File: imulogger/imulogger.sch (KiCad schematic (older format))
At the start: 31 parts, among them J1 DEBUG, J2 BATCONN, J4 Micro_SD_Card, J5 PWRCONN, Q1 TP0610T, U1 ESP32-WROOM-32, U2 USFS, U3 MCP1826S, U4 MCP73831-2-OT

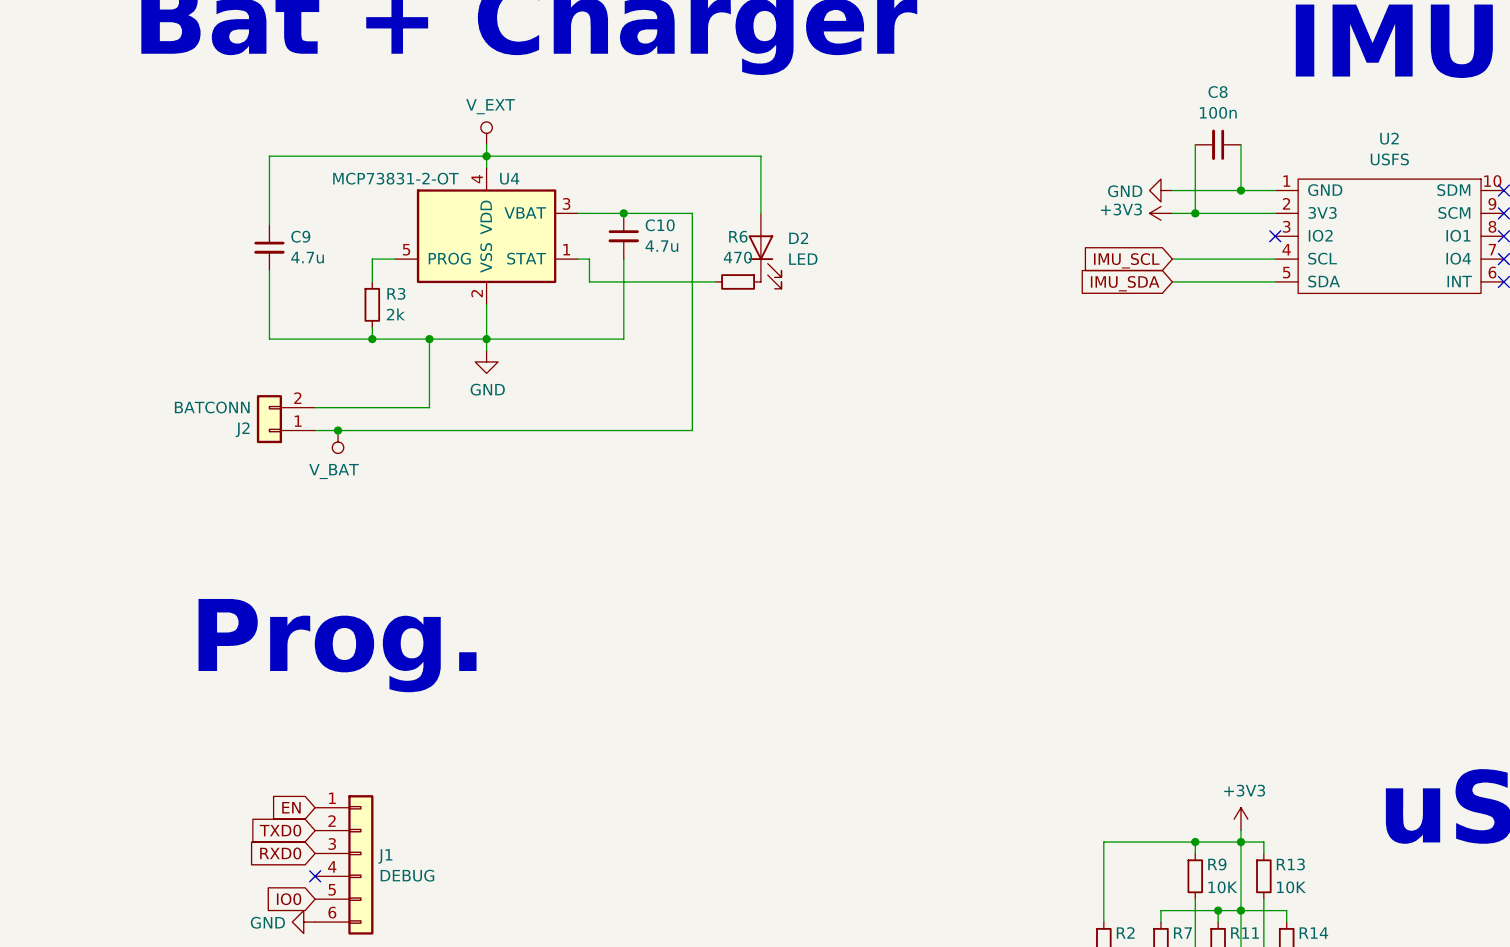
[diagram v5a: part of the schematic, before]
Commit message: imulogger: add battery protection circuit
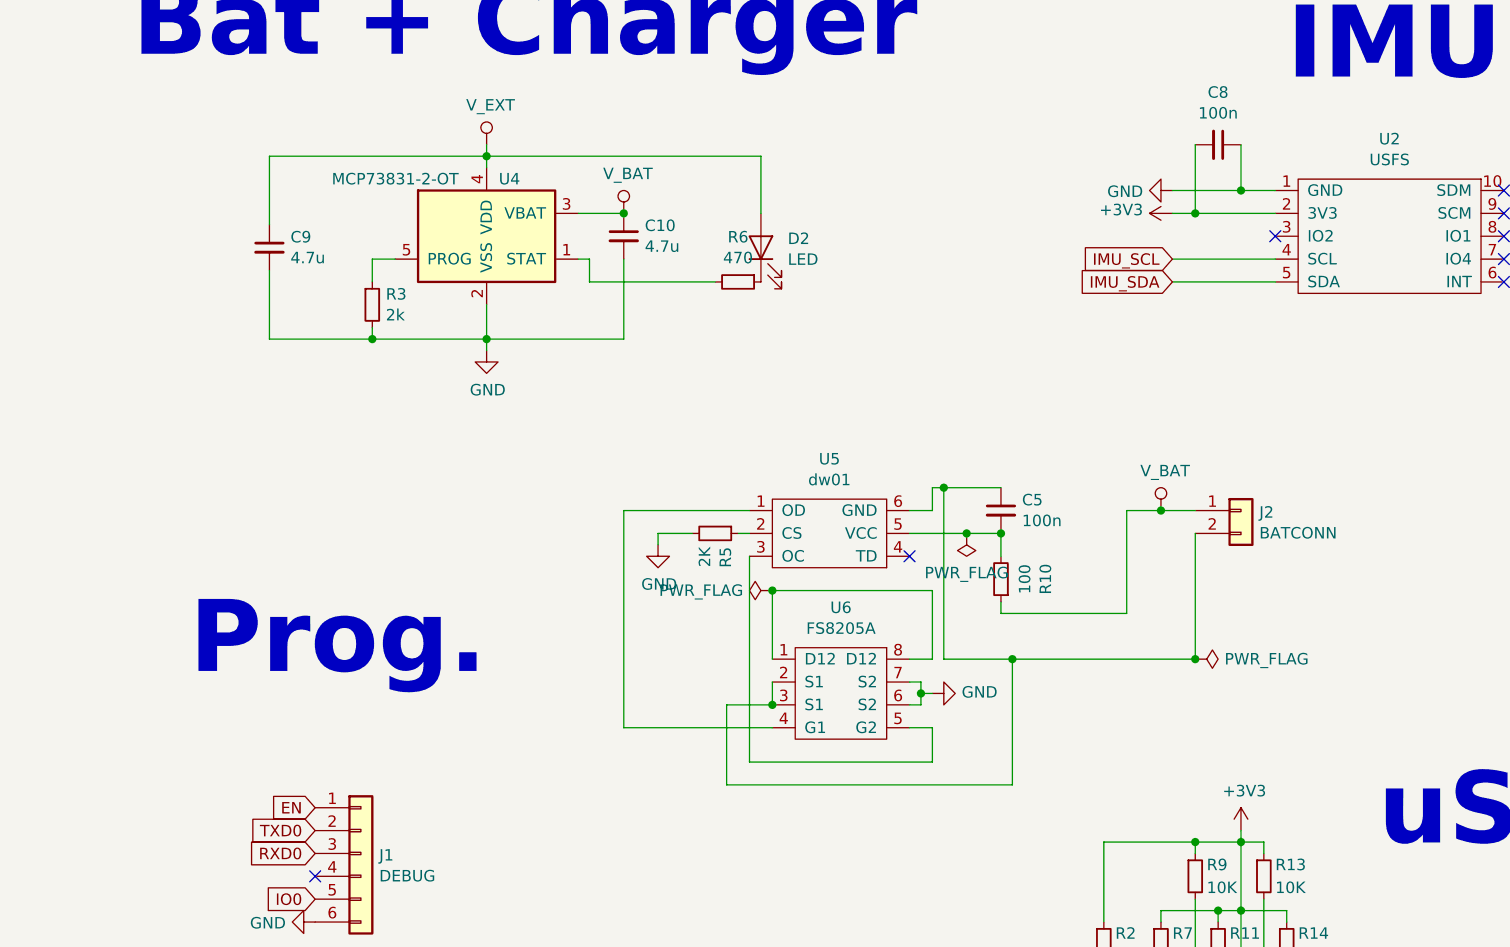
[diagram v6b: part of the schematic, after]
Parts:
- added C5: 100n, Capacitor_SMD:C_0805_2012Metric_Pad1.15x1.40mm_HandSolder, symbol Device:C_Small
- added R10: 100, Resistor_SMD:R_0805_2012Metric_Pad1.15x1.40mm_HandSolder, symbol Device:R_Small
- added R5: 2K, Resistor_SMD:R_0805_2012Metric_Pad1.15x1.40mm_HandSolder, symbol Device:R_Small
- added U5: dw01, Package_TO_SOT_SMD:SOT-23-6_Handsoldering, symbol imulogger-symbols:dw01
- added U6: FS8205A, Package_SO:TSSOP-8_4.4x3mm_P0.65mm, symbol imulogger-symbols:FS8205A
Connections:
- net GND: now also R5.2, U6.6 (S2), U6.7 (S2); no longer J2.2 (Pin_2)
- net V_BAT: now also R10.1
- new net: C5.1, J2.2 (Pin_2), U5.6 (GND), U6.2 (S1), U6.3 (S1)
- new net: C5.2, R10.2, U5.5 (VCC)
- new net: R5.1, U5.2 (CS)
- new net: U6.1 (D12), U6.8 (D12)
- new net: U5.1 (OD), U6.4 (G1)
- new net: U5.3 (OC), U6.5 (G2)
- no-connect marks 30 -> 31
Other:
- moved on the sheet: J2
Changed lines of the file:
@@
 Text Notes 1050 6200 0    315  ~ 63
 PwrSrcSel + Reg
-$Comp
-L Connector_Generic:Conn_01x02 J2
-U 1 1 5CBEA1D0
-P 4500 2700
-F 0 "J2" H 4580 2692 50  0000 L CNN
-F 1 "BATCONN" H 4580 2601 50  0000 L CNN
-F 2 "Connector_PinHeader_2.54mm:PinHeader_1x02_P2.54mm_Vertical" H 4500 2700 50  0001 C CNN
-F 3 "~" H 4500 2700 50  0001 C CNN
-	1    4500 2700
-	-1   0    0    1
-$EndComp
-Wire Wire Line
-	5200 2600 5200 2300
-Wire Wire Line
-	4950 2300 5200 2300
-Wire Wire Line
-	5200 2300 5450 2300
-Connection ~ 5200 2300
-Wire Wire Line
-	6350 2700 6350 1750
-Wire Wire Line
-	6350 1750 6050 1750
 Connection ~ 6050 1750
-Wire Wire Line
-	4700 2700 4800 2700
 $Comp
 L Device:D_Schottky D4
@@
 L imulogger-symbols:V_BAT #PWR06
 U 1 1 5CCA121B
-P 4800 2700
-F 0 "#PWR06" H 4800 2550 50  0001 C CNN
-F 1 "V_BAT" H 4818 2873 50  0000 C CNN
-F 2 "" H 4800 2700 50  0001 C CNN
-F 3 "" H 4800 2700 50  0001 C CNN
-	1    4800 2700
-	-1   0    0    1
-$EndComp
-Connection ~ 4800 2700
+P 6050 1750
+F 0 "#PWR06" H 6050 1600 50  0001 C CNN
+F 1 "V_BAT" H 6068 1923 50  0000 C CNN
+F 2 "" H 6050 1750 50  0001 C CNN
+F 3 "" H 6050 1750 50  0001 C CNN
+	1    6050 1750
+	1    0    0    -1
+$EndComp
 $Comp
 L imulogger-symbols:V_EXT #PWR011
@@
 Wire Wire Line
 	1250 6900 1300 6900
-Wire Wire Line
-	4800 2700 6350 2700
-Wire Wire Line
-	4700 2600 5200 2600
 $Comp
 L power:PWR_FLAG #FLG0103
@@
 NoConn ~ 9050 6150
 NoConn ~ 9050 6250
+$Comp
+L Device:R_Small R10
+U 1 1 5CD8A10E
+P 7700 3350
+F 0 "R10" V 7504 3350 50  0000 C CNN
+F 1 "100" V 7595 3350 50  0000 C CNN
+F 2 "Resistor_SMD:R_0805_2012Metric_Pad1.15x1.40mm_HandSolder" H 7700 3350 50  0001 C CNN
+F 3 "~" H 7700 3350 50  0001 C CNN
+	1    7700 3350
+	-1   0    0    1
+$EndComp
+$Comp
+L Device:R_Small R5
+U 1 1 5CD8A55A
+P 6450 3150
+F 0 "R5" H 6509 3196 50  0000 L CNN
+F 1 "2K" H 6509 3105 50  0000 L CNN
+F 2 "Resistor_SMD:R_0805_2012Metric_Pad1.15x1.40mm_HandSolder" H 6450 3150 50  0001 C CNN
+F 3 "~" H 6450 3150 50  0001 C CNN
+	1    6450 3150
+	0    1    1    0
+$EndComp
+$Comp
+L Device:C_Small C5
+U 1 1 5CD8AEEA
+P 7700 3050
+F 0 "C5" H 7792 3096 50  0000 L CNN
+F 1 "100n" H 7792 3005 50  0000 L CNN
+F 2 "Capacitor_SMD:C_0805_2012Metric_Pad1.15x1.40mm_HandSolder" H 7700 3050 50  0001 C CNN
+F 3 "~" H 7700 3050 50  0001 C CNN
+	1    7700 3050
+	1    0    0    -1
+$EndComp
+$Comp
+L imulogger-symbols:FS8205A U6
+U 1 1 5CD95DDA
+P 7000 3850
+F 0 "U6" H 7000 4225 50  0000 C CNN
+F 1 "FS8205A" H 7000 4134 50  0000 C CNN
+F 2 "Package_SO:TSSOP-8_4.4x3mm_P0.65mm" H 7000 3850 50  0001 C CNN
+F 3 "" H 7000 3850 50  0001 C CNN
+	1    7000 3850
+	1    0    0    -1
+$EndComp
+$Comp
+L imulogger-symbols:dw01 U5
+U 1 1 5CD9CC1D
+P 6950 3150
+F 0 "U5" V 6625 3150 50  0000 C CNN
+F 1 "dw01" V 6716 3150 50  0000 C CNN
+F 2 "Package_TO_SOT_SMD:SOT-23-6_Handsoldering" H 6950 3150 50  0001 C CNN
+F 3 "" H 6950 3150 50  0001 C CNN
+	1    6950 3150
+	0    1    1    0
+$EndComp
+Wire Wire Line
+	7300 3050 7400 3050
+Wire Wire Line
+	7400 3050 7400 2950
+Wire Wire Line
+	7400 2950 7450 2950
+NoConn ~ 7300 3250
+Wire Wire Line
+	7700 3150 7700 3250
+Connection ~ 7700 3150
+Wire Wire Line
+	6600 3150 6550 3150
+$Comp
+L Connector_Generic:Conn_01x02 J2
+U 1 1 5CBEA1D0
+P 8750 3050
+F 0 "J2" H 8830 3042 50  0000 L CNN
+F 1 "BATCONN" H 8830 2951 50  0000 L CNN
+F 2 "Connector_PinHeader_2.54mm:PinHeader_1x02_P2.54mm_Vertical" H 8750 3050 50  0001 C CNN
+F 3 "~" H 8750 3050 50  0001 C CNN
+	1    8750 3050
+	1    0    0    -1
+$EndComp
+Wire Wire Line
+	8550 3050 8400 3050
+Wire Wire Line
+	8250 3050 8250 3500
+Wire Wire Line
+	8250 3500 7700 3500
+Wire Wire Line
+	7700 3500 7700 3450
+Wire Wire Line
+	4950 2300 5450 2300
+$Comp
+L imulogger-symbols:V_BAT #PWR014
+U 1 1 5CDD3FAE
+P 8400 3050
+F 0 "#PWR014" H 8400 2900 50  0001 C CNN
+F 1 "V_BAT" H 8418 3223 50  0000 C CNN
+F 2 "" H 8400 3050 50  0001 C CNN
+F 3 "" H 8400 3050 50  0001 C CNN
+	1    8400 3050
+	1    0    0    -1
+$EndComp
+Connection ~ 8400 3050
+Wire Wire Line
+	8400 3050 8250 3050
+Wire Wire Line
+	6600 3050 6050 3050
+Wire Wire Line
+	6050 4000 6700 4000
+Wire Wire Line
+	6600 4150 7400 4150
+Wire Wire Line
+	7400 4150 7400 4000
+Wire Wire Line
+	7400 4000 7300 4000
+$Comp
+L power:GND #PWR012
+U 1 1 5CDE1482
+P 6200 3200
+F 0 "#PWR012" H 6200 2950 50  0001 C CNN
+F 1 "GND" H 6205 3027 50  0000 C CNN
+F 2 "" H 6200 3200 50  0001 C CNN
+F 3 "" H 6200 3200 50  0001 C CNN
+	1    6200 3200
+	1    0    0    -1
+$EndComp
+Wire Wire Line
+	6350 3150 6200 3150
+Wire Wire Line
+	6200 3150 6200 3200
+Wire Wire Line
+	8550 3150 8550 3700
+Wire Wire Line
+	8550 3700 7750 3700
+Wire Wire Line
+	7750 3700 7750 4250
+Wire Wire Line
+	7750 4250 6500 4250
+Wire Wire Line
+	6500 4250 6500 3900
+Wire Wire Line
+	6500 3900 6700 3900
+Wire Wire Line
+	6700 3800 6700 3900
+Connection ~ 6700 3900
+Wire Wire Line
+	7300 3700 7400 3700
+Wire Wire Line
+	7400 3700 7400 3400
+Wire Wire Line
+	7400 3400 6700 3400
+Wire Wire Line
+	6700 3400 6700 3700
+$Comp
+L power:GND #PWR013
+U 1 1 5CDF671F
+P 7400 3850
+F 0 "#PWR013" H 7400 3600 50  0001 C CNN
+F 1 "GND" V 7405 3722 50  0000 R CNN
+F 2 "" H 7400 3850 50  0001 C CNN
+F 3 "" H 7400 3850 50  0001 C CNN
+	1    7400 3850
+	0    -1   -1   0
+$EndComp
+Wire Wire Line
+	7300 3800 7350 3800
+Wire Wire Line
+	7350 3800 7350 3850
+Wire Wire Line
+	7350 3850 7400 3850
+Wire Wire Line
+	7300 3900 7350 3900
+Wire Wire Line
+	7350 3900 7350 3850
+Connection ~ 7350 3850
+$Comp
+L power:PWR_FLAG #FLG0105
+U 1 1 5CE03E12
+P 8550 3700
+F 0 "#FLG0105" H 8550 3775 50  0001 C CNN
+F 1 "PWR_FLAG" V 8550 3828 50  0000 L CNN
+F 2 "" H 8550 3700 50  0001 C CNN
+F 3 "~" H 8550 3700 50  0001 C CNN
+	1    8550 3700
+	0    1    1    0
+$EndComp
+Wire Wire Line
+	7450 3700 7750 3700
+Connection ~ 7450 2950
+Wire Wire Line
+	7450 2950 7700 2950
+Connection ~ 7750 3700
+Connection ~ 8550 3700
+Wire Wire Line
+	7450 2950 7450 3700
+Wire Wire Line
+	7700 3150 7550 3150
+$Comp
+L power:PWR_FLAG #FLG0106
+U 1 1 5CE0DB17
+P 7550 3150
+F 0 "#FLG0106" H 7550 3225 50  0001 C CNN
+F 1 "PWR_FLAG" H 7550 3323 50  0000 C CNN
+F 2 "" H 7550 3150 50  0001 C CNN
+F 3 "~" H 7550 3150 50  0001 C CNN
+	1    7550 3150
+	-1   0    0    1
+$EndComp
+Connection ~ 7550 3150
+Wire Wire Line
+	7550 3150 7300 3150
+Wire Wire Line
+	6050 3050 6050 4000
+Wire Wire Line
+	6600 3250 6600 4150
+$Comp
+L power:PWR_FLAG #FLG0107
+U 1 1 5CE12164
+P 6700 3400
+F 0 "#FLG0107" H 6700 3475 50  0001 C CNN
+F 1 "PWR_FLAG" V 6700 3527 50  0000 L CNN
+F 2 "" H 6700 3400 50  0001 C CNN
+F 3 "~" H 6700 3400 50  0001 C CNN
+	1    6700 3400
+	0    -1   -1   0
+$EndComp
+Connection ~ 6700 3400
 $EndSCHEMATC

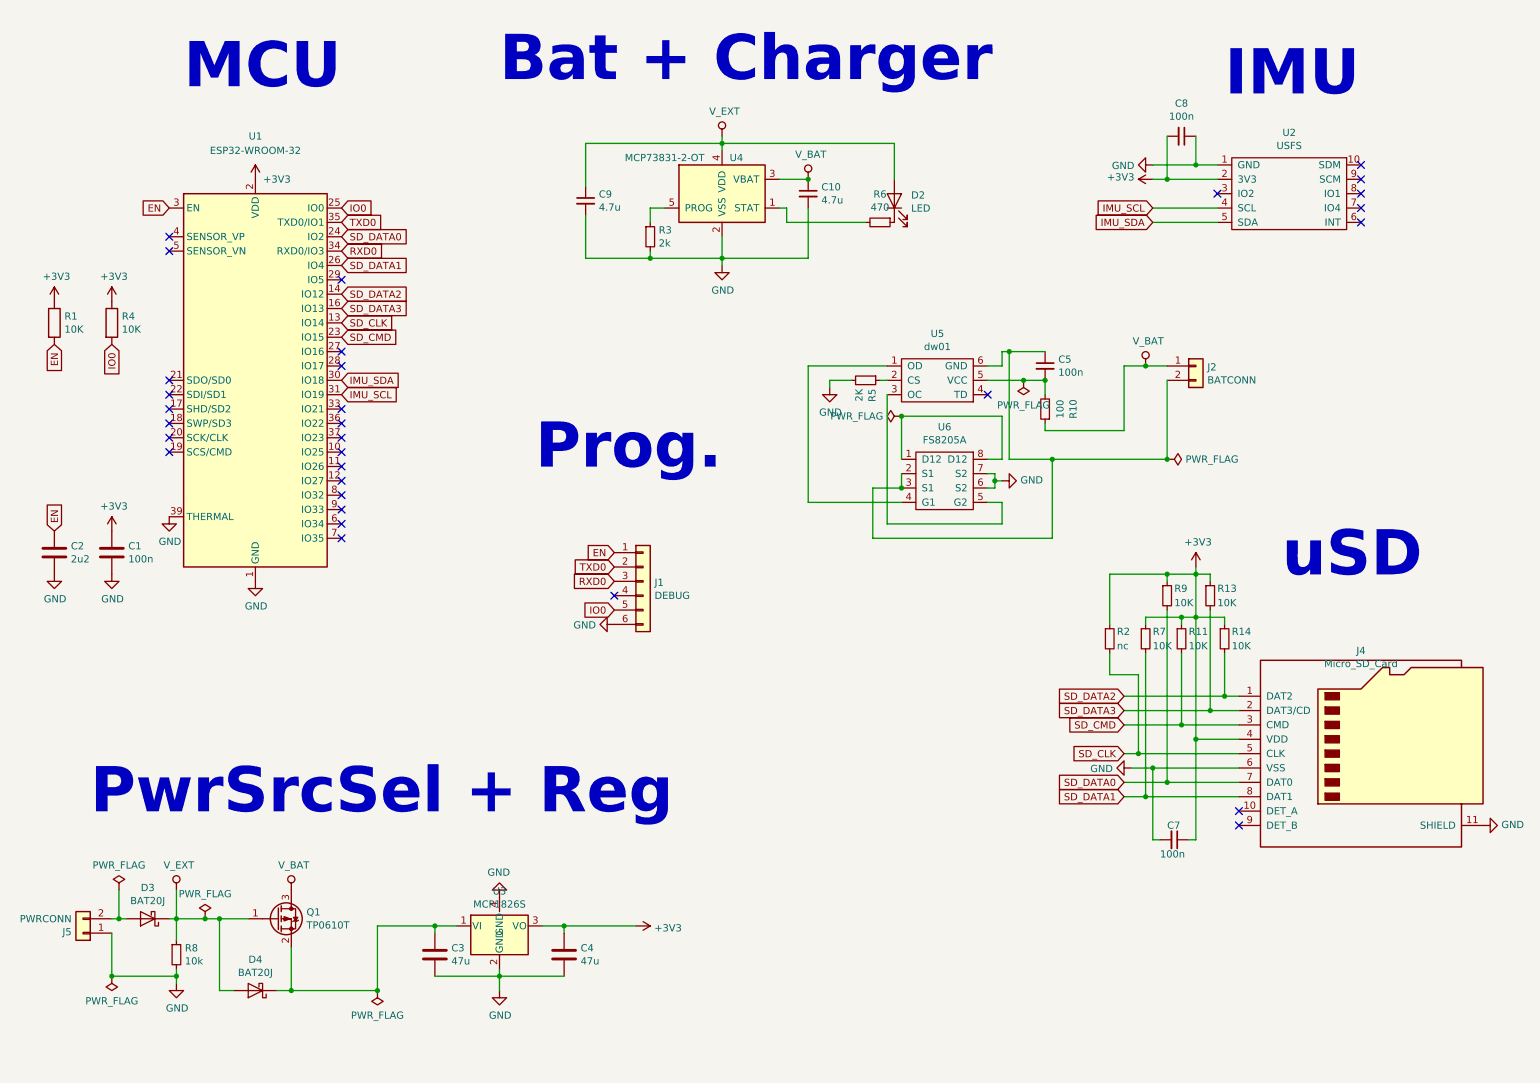
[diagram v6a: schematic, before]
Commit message: remove charger and add switch and JST socket
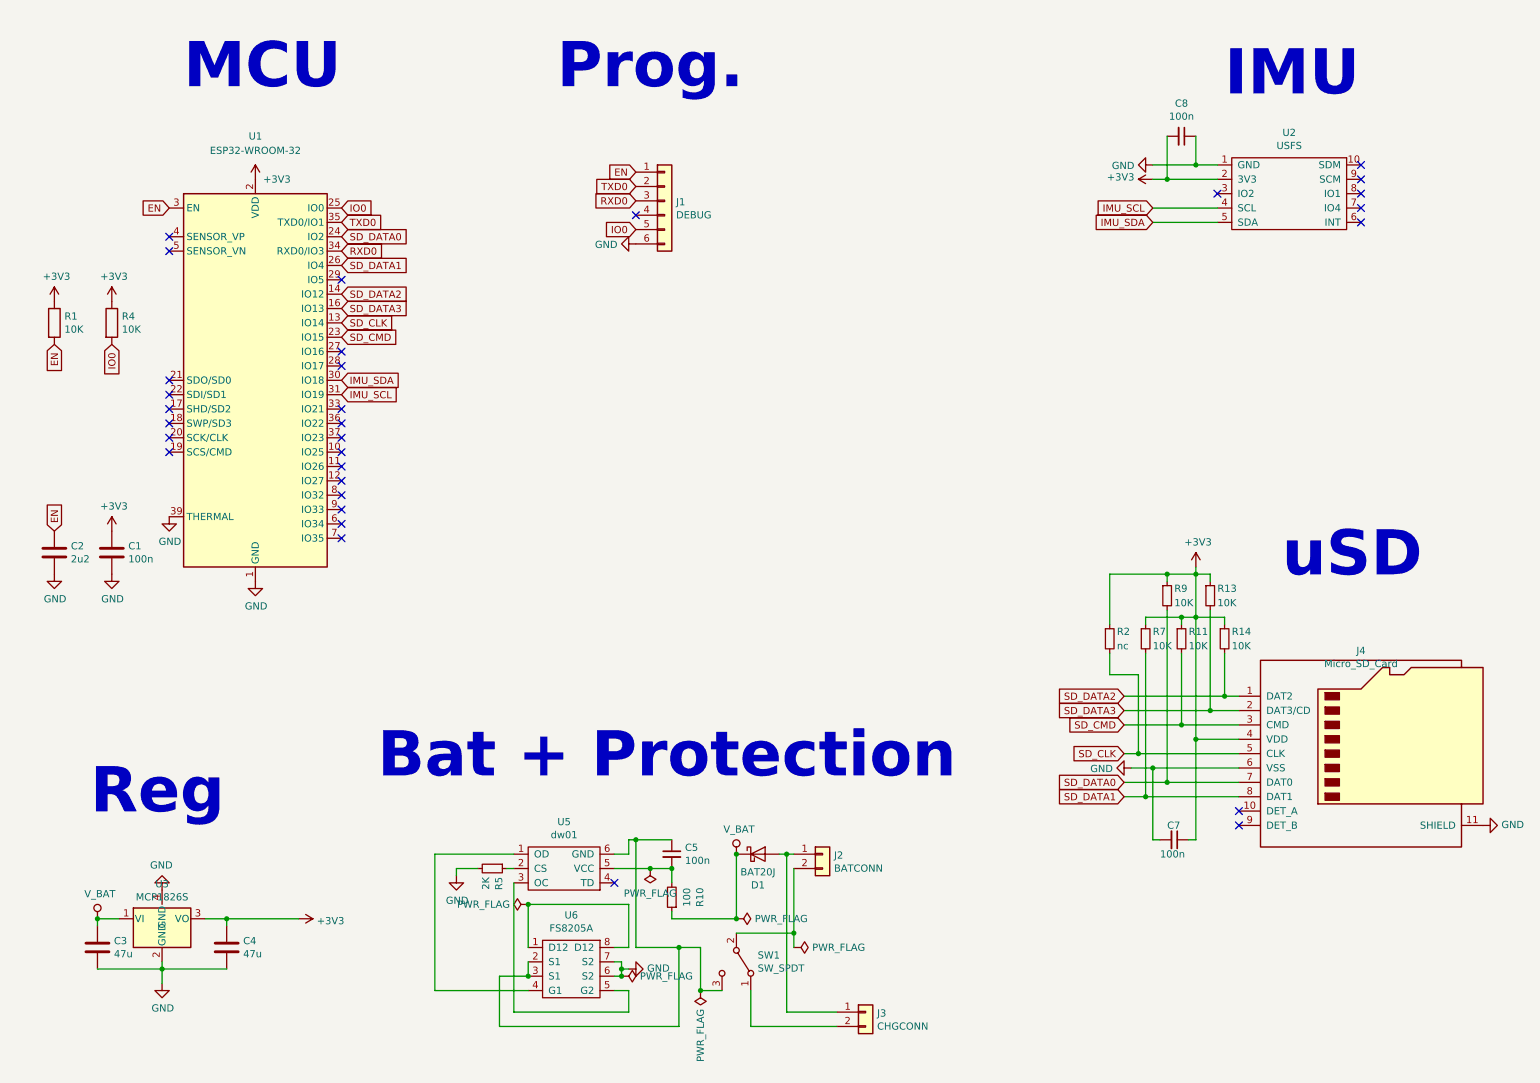
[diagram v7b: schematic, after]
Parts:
- removed C10, C9: 4.7u, Capacitor_SMD:C_0805_2012Metric_Pad1.15x1.40mm_HandSolder, symbol Device:C_Small
- removed D2: LED, LED_SMD:LED_0805_2012Metric_Pad1.15x1.40mm_HandSolder, symbol Device:LED
- removed D3, D4: BAT20J, Diode_SMD:D_SOD-323, symbol Device:D_Schottky
- removed J5: PWRCONN, Connector_PinHeader_2.54mm:PinHeader_1x02_P2.54mm_Vertical, symbol Connector_Generic:Conn_01x02
- removed Q1: TP0610T, Package_TO_SOT_SMD:SOT-23, symbol Transistor_FET:TP0610T
- removed R3: 2k, Resistor_SMD:R_0805_2012Metric_Pad1.15x1.40mm_HandSolder, symbol Device:R_Small
- removed R6: 470, Resistor_SMD:R_0805_2012Metric_Pad1.15x1.40mm_HandSolder, symbol Device:R_Small
- removed R8: 10k, Resistor_SMD:R_0805_2012Metric_Pad1.15x1.40mm_HandSolder, symbol Device:R_Small
- removed U4: MCP73831-2-OT, Package_TO_SOT_SMD:SOT-23-5, symbol Battery_Management:MCP73831-2-OT
- added D1: BAT20J, Diode_SMD:D_SOD-323, symbol Device:D_Schottky
- added J3: CHGCONN, Connector_JST:JST_PH_S2B-PH-K_1x02_P2.00mm_Horizontal, symbol Connector_Generic:Conn_01x02
- added SW1: SW_SPDT, imulogger-footprints:SK-3296S-01-L3, symbol Switch:SW_SPDT
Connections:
- net V_BAT: now also C3.1, U3.1 (VI), D1.1 (K); no longer J2.1 (Pin_1)
- net at C5.1, U5.6 (GND), U6.2 (S1)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: now also SW1.3 (C); no longer J2.2 (Pin_2)
- new net: D1.2 (A), J2.1 (Pin_1), J3.1 (Pin_1)
- new net: J2.2 (Pin_2), SW1.2 (B)
- new net: J3.2 (Pin_2), SW1.1 (A)
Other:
- note added: "Bat + Protection"
- note added: "Reg"
- note removed: "Bat + Charger"
- note removed: "PwrSrcSel + Reg"
- moved on the sheet: C3, C4, C5, J1, J2, R10, R5, U3, U5, U6
